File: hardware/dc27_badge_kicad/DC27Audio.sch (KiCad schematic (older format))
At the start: 22 parts, among them U501 CS4344-CZZ, U502 LM4880

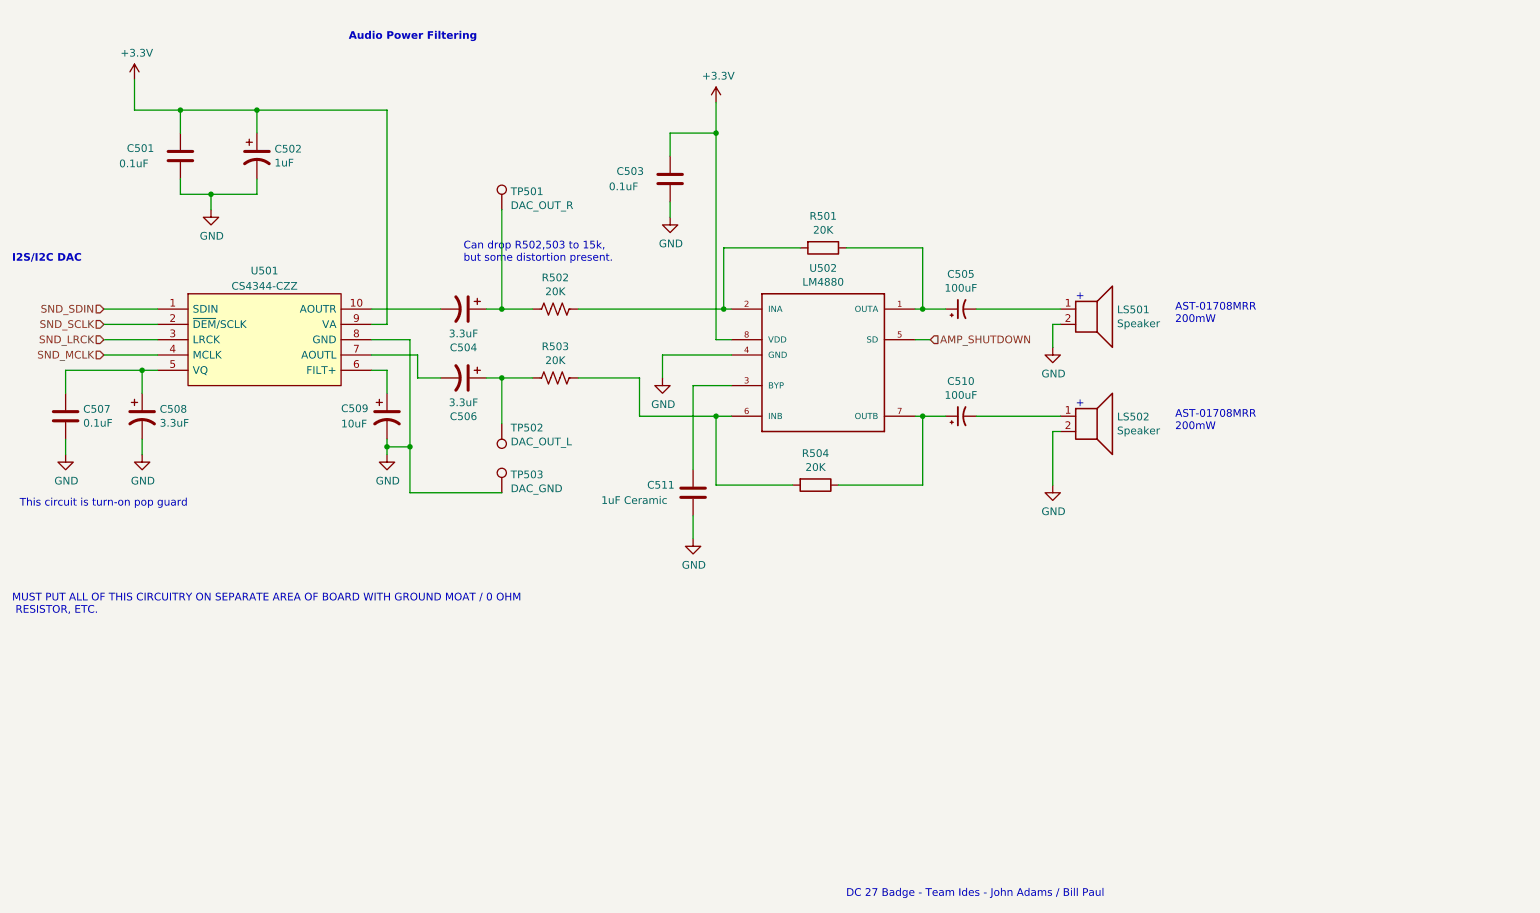
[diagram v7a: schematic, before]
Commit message: update schematic and pcb with proper audio cap polarity
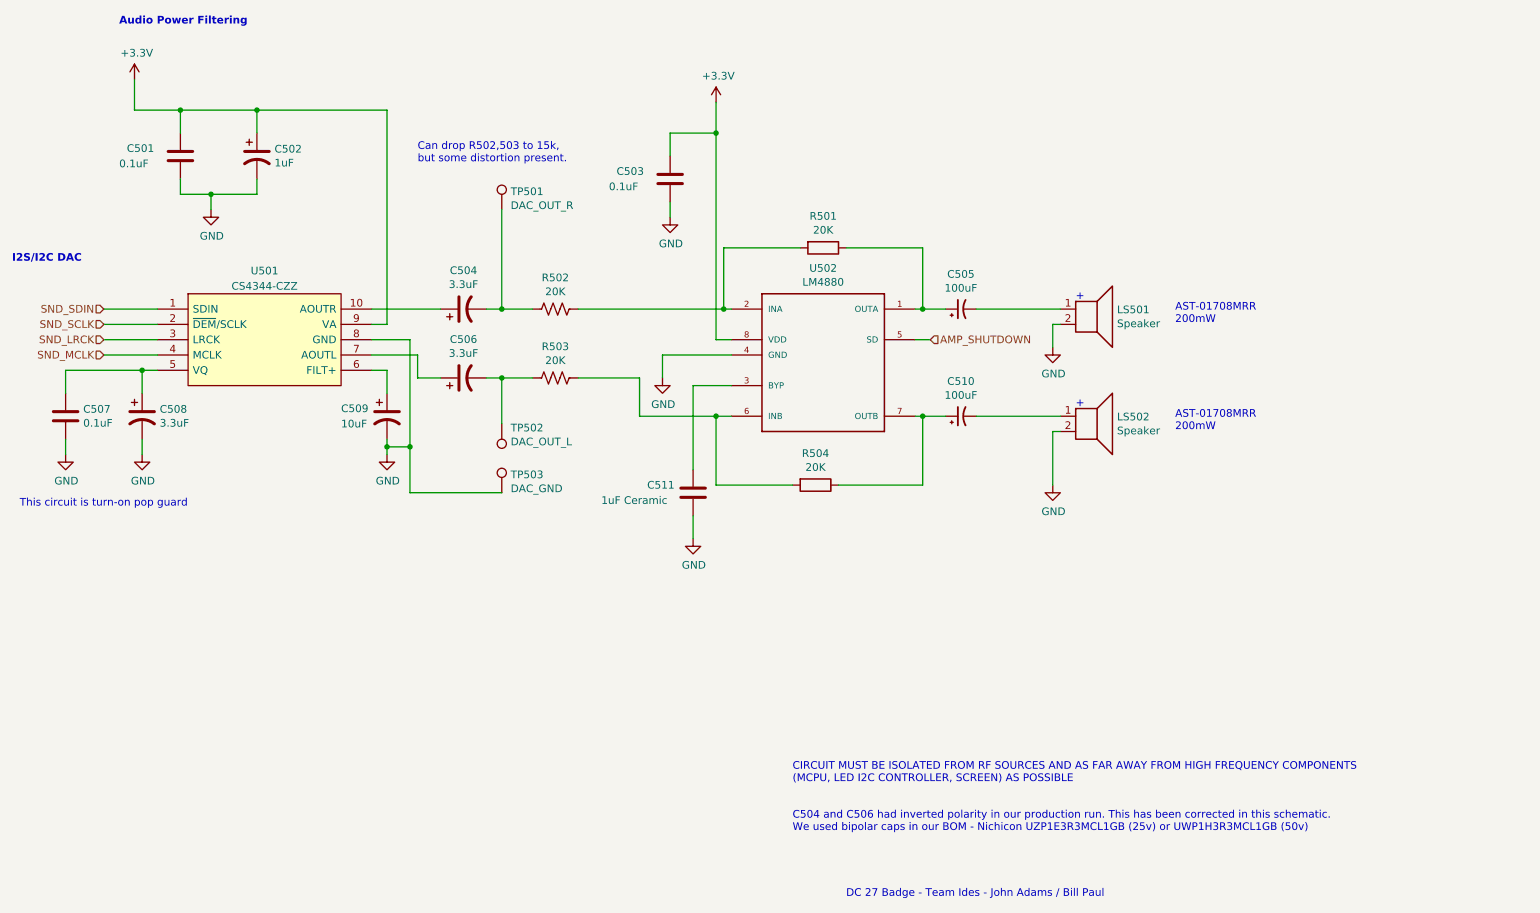
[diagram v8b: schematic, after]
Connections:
- net at R503.2, TP502.1: now also C506.2; no longer C506.1
- net at R502.2, TP501.1: now also C504.2; no longer C504.1
- net at U501.10 (AOUTR): now also C504.1; no longer C504.2
- net at U501.7 (AOUTL): now also C506.1; no longer C506.2
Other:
- note added: "C504 and C506 had inverted polarity in our production run. This has been corrected in this schematic. \nWe used bipolar caps in our BOM - Nichicon UZP1E3R3MCL1GB (25v) or UWP1H3R3MCL1GB (50v)\n\n"
- note added: "CIRCUIT MUST BE ISOLATED FROM RF SOURCES AND AS FAR AWAY FROM HIGH FREQUENCY COMPONENTS \n(MCPU, LED I2C CONTROLLER, SCREEN) AS POSSIBLE"
- note removed: "MUST PUT ALL OF THIS CIRCUITRY ON SEPARATE AREA OF BOARD WITH GROUND MOAT / 0 OHM\n RESISTOR, ETC."
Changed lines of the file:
@@
 Text Notes 1900 3350 0    50   ~ 10
 I2S/I2C DAC
-Text Notes 4100 1900 0    50   ~ 10
+Text Notes 2600 1800 0    50   ~ 10
 Audio Power Filtering\n
 Text Notes 8850 4300 0    50   ~ 0
@@
 	0    1    1    0
 $EndComp
-Text Notes 1900 5650 0    50   ~ 0
-MUST PUT ALL OF THIS CIRCUITRY ON SEPARATE AREA OF BOARD WITH GROUND MOAT / 0 OHM\n RESISTOR, ETC.
+Text Notes 7000 6750 0    50   ~ 0
+CIRCUIT MUST BE ISOLATED FROM RF SOURCES AND AS FAR AWAY FROM HIGH FREQUENCY COMPONENTS \n(MCPU, LED I2C CONTROLLER, SCREEN) AS POSSIBLE
 $Comp
 L Device:C C511
@@
 F 3 "~" H 4850 3650 50  0001 C CNN
 	1    4850 3650
-	0    1    1    0
+	0    -1   -1   0
 $EndComp
 $Comp
@@
 F 3 "~" H 4850 4100 50  0001 C CNN
 	1    4850 4100
-	0    1    1    0
+	0    -1   -1   0
 $EndComp
 $Comp
@@
 Text Notes 9500 4450 0    50   ~ 0
 AST-01708MRR\n200mW
-Text Notes 4850 3350 0    50   ~ 0
+Text Notes 4550 2700 0    50   ~ 0
 Can drop R502,503 to 15k, \nbut some distortion present.
 $Comp
@@
 	4500 4850 4500 4550
 Connection ~ 4500 4550
+Text Notes 7000 7150 0    50   ~ 0
+C504 and C506 had inverted polarity in our production run. This has been corrected in this schematic. \nWe used bipolar caps in our BOM - Nichicon UZP1E3R3MCL1GB (25v) or UWP1H3R3MCL1GB (50v)\n\n
 $EndSCHEMATC
